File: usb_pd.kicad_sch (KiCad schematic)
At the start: 81 parts, among them Q1 Q_Dual_NMOS, Q2 Q_Dual_NMOS, U5 TPS5403DR, U6 MP28167GQ-P, U7 BQ25731

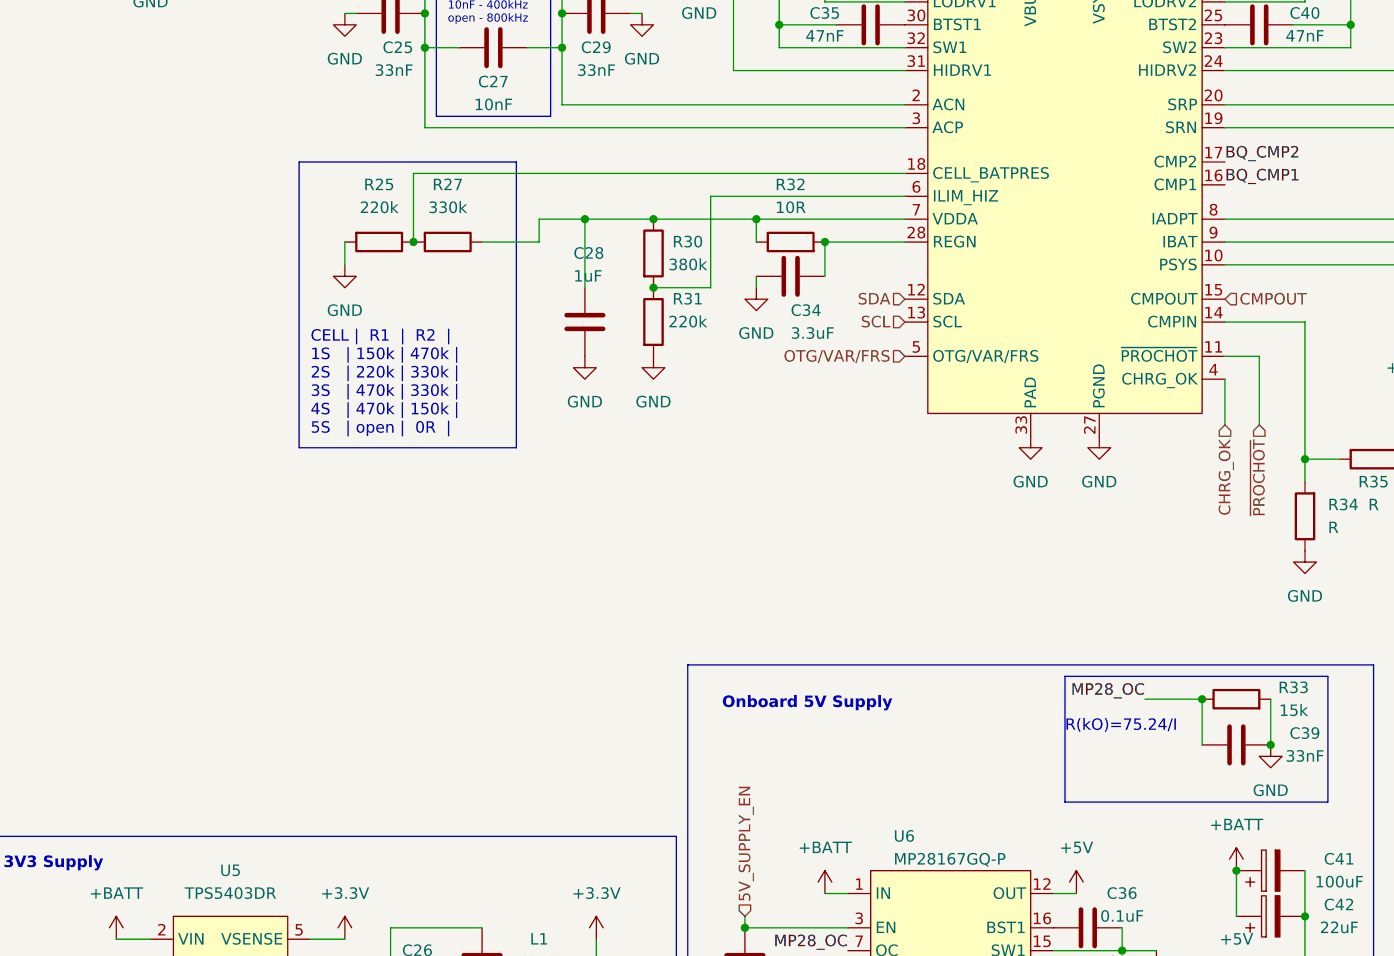
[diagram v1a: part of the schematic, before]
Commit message: minor setting changes in schematics, added test software container
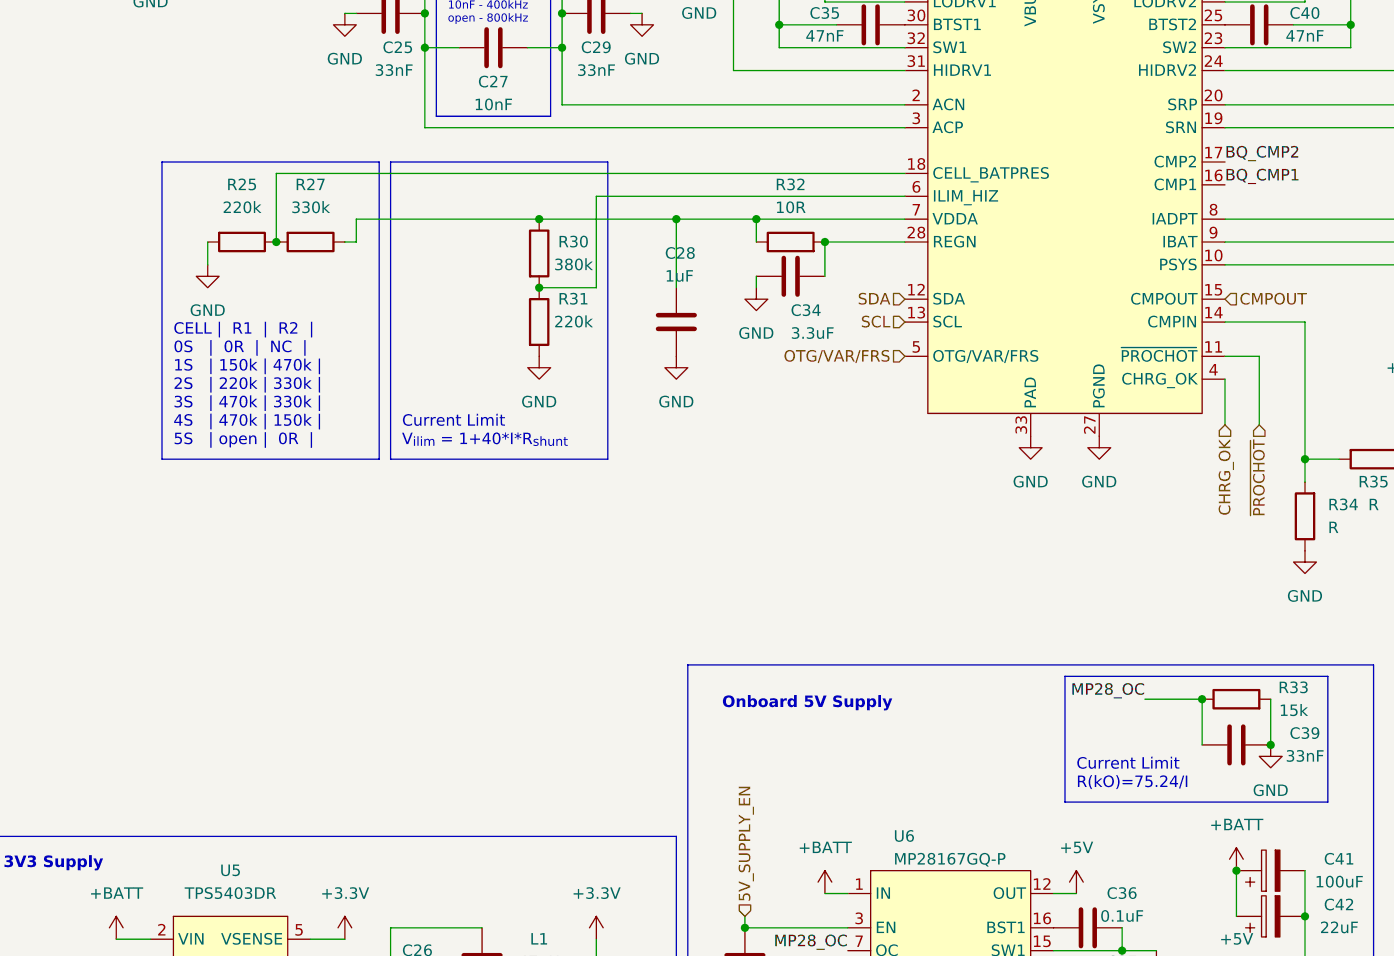
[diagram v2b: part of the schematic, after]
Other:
- note added: "CELL | R1 | R2 | 0S | 0R | NC | 1S | 150k | 470k | 2S | 220k | 330k | 3S | 470k | 330k | 4S | 470k | 150k | 5S | open | 0R |"
- note added: "Current Limit R(kO)=75.24/I"
- note added: "Current Limit V_{ilim} = 1+40*I*R_{shunt}"
- note removed: "CELL | R1 | R2 | 1S | 150k | 470k | 2S | 220k | 330k | 3S | 470k | 330k | 4S | 470k | 150k | 5S | open | 0R |"
- note removed: "R(kO)=75.24/I"
- moved on the sheet: C28, R25, R27, R30, R31
